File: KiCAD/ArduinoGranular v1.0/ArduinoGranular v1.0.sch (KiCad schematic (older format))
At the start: 51 parts, among them J1 GRAIN2_DECAY, J2 GRAIN1_FREQ, J3 GRAIN1_DECAY, J4 GRAIN2_FREQ, J5 SYNC, J6 OUTPUT, U4 TL074, U5 TL072, U6 ADS1115IDGS

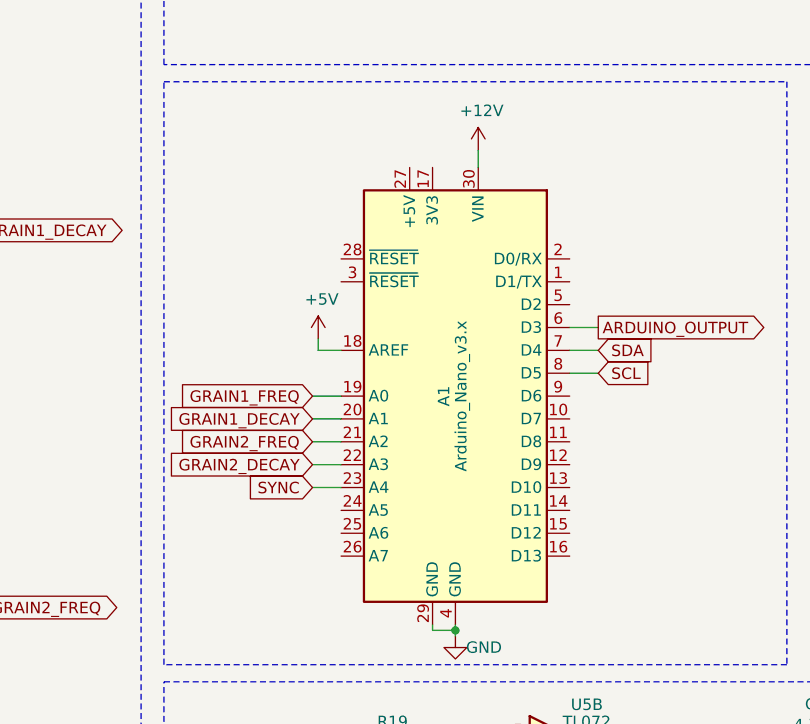
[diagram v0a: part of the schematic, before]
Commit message: Marked NCs, fixed IDC bus grounds
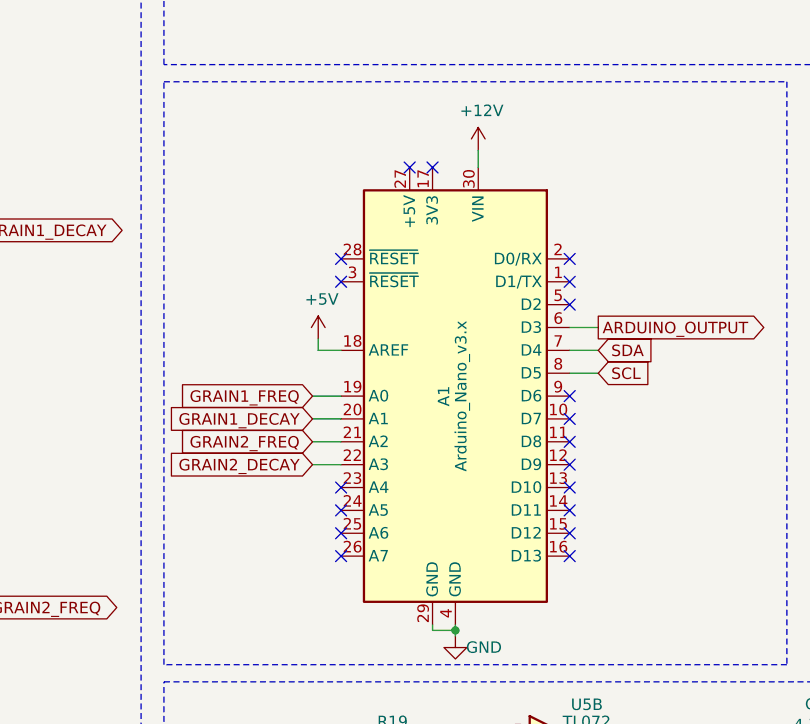
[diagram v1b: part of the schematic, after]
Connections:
- net SYNC: no longer names the net of A1.23 (A4)
- no-connect marks 7 -> 26
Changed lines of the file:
@@
 Wire Wire Line
 	6000 4300 6125 4300
-Text GLabel 6000 4400 0    50   Input ~ 0
-SYNC
-Wire Wire Line
-	6000 4400 6125 4400
 Text GLabel 7250 3700 2    50   Output ~ 0
 ARDUINO_OUTPUT
@@
 	1    0    0    1
 $EndComp
+NoConn ~ 6425 3000
+NoConn ~ 6525 3000
+NoConn ~ 6125 3400
+NoConn ~ 6125 3500
+NoConn ~ 7125 3400
+NoConn ~ 7125 3500
+NoConn ~ 7125 3600
+NoConn ~ 7125 4000
+NoConn ~ 7125 4100
+NoConn ~ 7125 4200
+NoConn ~ 7125 4300
+NoConn ~ 7125 4400
+NoConn ~ 7125 4500
+NoConn ~ 7125 4600
+NoConn ~ 7125 4700
+NoConn ~ 6125 4500
+NoConn ~ 6125 4600
+NoConn ~ 6125 4700
+NoConn ~ 6125 4400
 $EndSCHEMATC
